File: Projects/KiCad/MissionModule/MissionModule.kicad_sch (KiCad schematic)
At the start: 23 parts, among them J1 Conn_01x04_Pin, J2 Conn_01x04_Pin, J3 Micro_SD_Card_Det_Hirose_DM3AT, U1 ABX00012, U2 MCP2562-E-P, U3 LT1584-3.3, U4 TLP222A, U5 MCP2515-I/P, Y1 8MHz

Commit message: ADXL375のCSをGNDに接続
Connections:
- net GND: now also U6.4 (SDO/ALT_ADDRESS)
- no-connect marks 26 -> 25
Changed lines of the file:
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@@
   (no_connect (at 60.96 118.11))
   (no_connect (at 123.19 161.29))
-  (no_connect (at 82.55 163.83))
   (no_connect (at 60.96 107.95))
   (no_connect (at 60.96 105.41))
@@
   )
   (wire (pts (xy 60.96 107.95) (xy 63.5 107.95))
+    (stroke (width 0) (type default))
+  )
+  (wire (pts (xy 82.55 163.83) (xy 82.55 168.91))
     (stroke (width 0) (type default))
   )
@@
         )
       )
+    )
+  )
+  (symbol (lib_id "power:GND") (at 82.55 168.91 0) (unit 1)
+    (in_bom yes) (on_board yes) (dnp no) (fields_autoplaced)
+    (property "Reference" "#PWR026" (at 82.55 175.26 0)
+      (effects (font (size 1.27 1.27)) hide)
+    )
+    (property "Value" "GND" (at 82.55 173.99 0)
+      (effects (font (size 1.27 1.27)))
+    )
+    (property "Footprint" "" (at 82.55 168.91 0)
+      (effects (font (size 1.27 1.27)) hide)
+    )
+    (property "Datasheet" "" (at 82.55 168.91 0)
+      (effects (font (size 1.27 1.27)) hide)
+    )
+    (pin "1")
+    (instances
+      (project "MissionModule"
+        (path "/ea1ed597-7cd3-4340-902e-bdce8f2d7a62"
+          (reference "#PWR026") (unit 1)
+        )
+      )

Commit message: 全モジュールのkicadを一通り作った
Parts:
- removed C3, C4: 0.1μF, Capacitor_SMD:C_0805_2012Metric_Pad1.18x1.45mm_HandSolder, symbol Device:C
- removed D1: 1N4148, Diode_THT:D_DO-35_SOD27_P7.62mm_Horizontal, symbol Diode:1N4148
- removed U3: LT1584-3.3, Package_TO_SOT_THT:TO-220-3_Vertical, symbol Regulator_Linear:LT1584-3.3
- added C3: 470μF, Capacitor_THT:CP_Radial_D10.0mm_P3.50mm, symbol Device:C_Polarized
- added D1, D2, D3, D4, D5, D6: LED, LED_SMD:LED_1206_3216Metric_Pad1.42x1.75mm_HandSolder, symbol Device:LED
- added R10, R11, R12, R9: 100Ω, Resistor_SMD:R_0805_2012Metric_Pad1.20x1.40mm_HandSolder, symbol Device:R
- added R13: 1kΩ, Resistor_SMD:R_0805_2012Metric_Pad1.20x1.40mm_HandSolder, symbol Device:R
- added R3, R7, R8: 4.7kΩ, Resistor_SMD:R_0805_2012Metric_Pad1.20x1.40mm_HandSolder, symbol Device:R
- added R6: 2kΩ, Resistor_SMD:R_0805_2012Metric_Pad1.20x1.40mm_HandSolder, symbol Device:R
- added SW1, SW2: SW_Push, Button_Switch_THT:SW_PUSH_6mm, symbol Switch:SW_Push
- added U6, U7: MB85RS2MT, Package_DIP:DIP-8_W7.62mm, symbol Memory_NVRAM:MB85RS2MT
- R2: footprint (none) -> Resistor_SMD:R_0805_2012Metric_Pad1.20x1.40mm_HandSolder
- renumbered C5 to C4, C6 to C5, C7 to C6, R3 to R4, R4 to R5, U6 to U1, U1 to U2, U2 to U3
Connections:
- net +3.3V: now also F1.1, C3.1, R3.1, R7.1, R8.1
- net +5V: now also R6.1
- net GND: now also J3.9 (DET_B), C3.2, D1.1 (K), D2.1 (K), D3.1 (K), D4.1 (K), D5.1 (K), D6.1 (K), SW1.1, SW2.1, U6.3 (~{WP}), U6.4 (GND), U6.7 (~{HOLD}), U7.3 (~{WP}), U7.4 (GND), U7.7 (~{HOLD})
- net MEMORY_POWER: now also R13.1, U6.8 (VDD), U7.8 (VDD)
- net SPI_CS_SD: now also R3.2
- net SPI_MISO: now also U6.2 (SO), U7.2 (SO)
- net SPI_MOSI: now also U6.5 (SI), U7.5 (SI)
- net SPI_SCLK: now also U6.6 (SCK), U7.6 (SCK)
- net CAN_SEND_STATUS: now reaches U2.10 (PA23_TC4-W1/1)
- net CAN_SEND_STATUS: now also R10.1
- net RECORD_STATUS: now reaches U2.11 (PA10_TCC0-W2/~2)
- net RECORD_STATUS: now also R11.1
- net SD_CHECK: now reaches U2.12 (PA11_TCC0-W3/~3)
- net SD_CHECK: now also J3.10 (DET_A)
- net SD_STATUS: now reaches U2.13 (PB10_TCC0-W4/~4)
- net SD_STATUS: now also R12.1
- net DUMP_MODE: now reaches U2.5 (PA04_AIN4/A3)
- net DUMP_MODE: now also SW2.2
- net DEBUG_MODE: now reaches U2.6 (PA05_AIN5/A4)
- net DEBUG_MODE: now also SW1.2
- net SPI_CS_FRAM1: now reaches U2.7 (PA06_AIN6/A5)
- net SPI_CS_FRAM1: now also R7.2, U6.1 (~{CS})
- net SPI_CS_FRAM0: now reaches U2.8 (PA07_AIN7/A6)
- net SPI_CS_FRAM0: now also R8.2, U7.1 (~{CS})
- net CAN_RECEIVE_STATUS: now reaches U2.9 (PA22_TC4-W0/0)
- net CAN_RECEIVE_STATUS: now also R9.1
- new net: D1.2 (A), R6.2
- new net: D5.2 (A), R12.2
- new net: D4.2 (A), R11.2
- new net: D3.2 (A), R10.2
- new net: D6.2 (A), R13.2
- new net: D2.2 (A), R9.2
- no-connect marks 25 -> 21
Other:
- moved on the sheet: C1, C2, C4, C5, C6, F1, J3, R1, R2, R4, R5, U1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

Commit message: 一通り部品を選定
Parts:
- added D7, D8: ORANGE, LED_SMD:LED_0603_1608Metric_Pad1.05x0.95mm_HandSolder, symbol Device:LED
- added R14, R15: 100Ω, Resistor_SMD:R_0603_1608Metric_Pad0.98x0.95mm_HandSolder, symbol Device:R
- C3: value 470μF -> 100μF; footprint Capacitor_THT:CP_Radial_D10.0mm_P3.50mm -> Capacitor_SMD:CP_Elec_6.3x7.7
- C5, C6: footprint Capacitor_SMD:C_0805_2012Metric_Pad1.18x1.45mm_HandSolder -> Capacitor_SMD:C_0603_1608Metric_Pad1.08x0.95mm_HandSolder
- D1, D6: value LED -> RED; footprint LED_SMD:LED_1206_3216Metric_Pad1.42x1.75mm_HandSolder -> LED_SMD:LED_0603_1608Metric_Pad1.05x0.95mm_HandSolder
- D2, D3: value LED -> ORANGE; footprint LED_SMD:LED_1206_3216Metric_Pad1.42x1.75mm_HandSolder -> LED_SMD:LED_0603_1608Metric_Pad1.05x0.95mm_HandSolder
- D4, D5: value LED -> GREEN; footprint LED_SMD:LED_1206_3216Metric_Pad1.42x1.75mm_HandSolder -> LED_SMD:LED_0603_1608Metric_Pad1.05x0.95mm_HandSolder
- F1: footprint Fuse:Fuse_BelFuse_0ZRE0005FF_L8.3mm_W3.8mm -> Fuse:Fuse_1206_3216Metric_Pad1.42x1.75mm_HandSolder
- R1: value 120R1/4W -> 120Ω; footprint Resistor_SMD:R_0805_2012Metric_Pad1.20x1.40mm_HandSolder -> Resistor_SMD:R_0603_1608Metric_Pad0.98x0.95mm_HandSolder
- R10, R2, R3, R4, R5, R7, R8, R9: footprint Resistor_SMD:R_0805_2012Metric_Pad1.20x1.40mm_HandSolder -> Resistor_SMD:R_0603_1608Metric_Pad0.98x0.95mm_HandSolder
- R11, R12: value 100Ω -> 300Ω; footprint Resistor_SMD:R_0805_2012Metric_Pad1.20x1.40mm_HandSolder -> Resistor_SMD:R_0603_1608Metric_Pad0.98x0.95mm_HandSolder
- R13: value 1kΩ -> 300Ω; footprint Resistor_SMD:R_0805_2012Metric_Pad1.20x1.40mm_HandSolder -> Resistor_SMD:R_0603_1608Metric_Pad0.98x0.95mm_HandSolder
- R6: value 2kΩ -> 620Ω; footprint Resistor_SMD:R_0805_2012Metric_Pad1.20x1.40mm_HandSolder -> Resistor_SMD:R_0603_1608Metric_Pad0.98x0.95mm_HandSolder
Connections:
- net GND: now also D7.1 (K), D8.1 (K)
- net LORA_SEND_STATUS: now reaches U2.3 (PB02_AIN10/A1)
- net LORA_SEND_STATUS: now also R15.1
- net LORA_RECEIVE_STATUS: now reaches U2.4 (PB03_AIN11/A2)
- net LORA_RECEIVE_STATUS: now also R14.1
- new net: D7.2 (A), R14.2
- new net: D8.2 (A), R15.2
- no-connect marks 21 -> 19
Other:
- moved on the sheet: C1, C2, C4, D1, D2, D3, D4, D5, D6, J1, J2, R1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

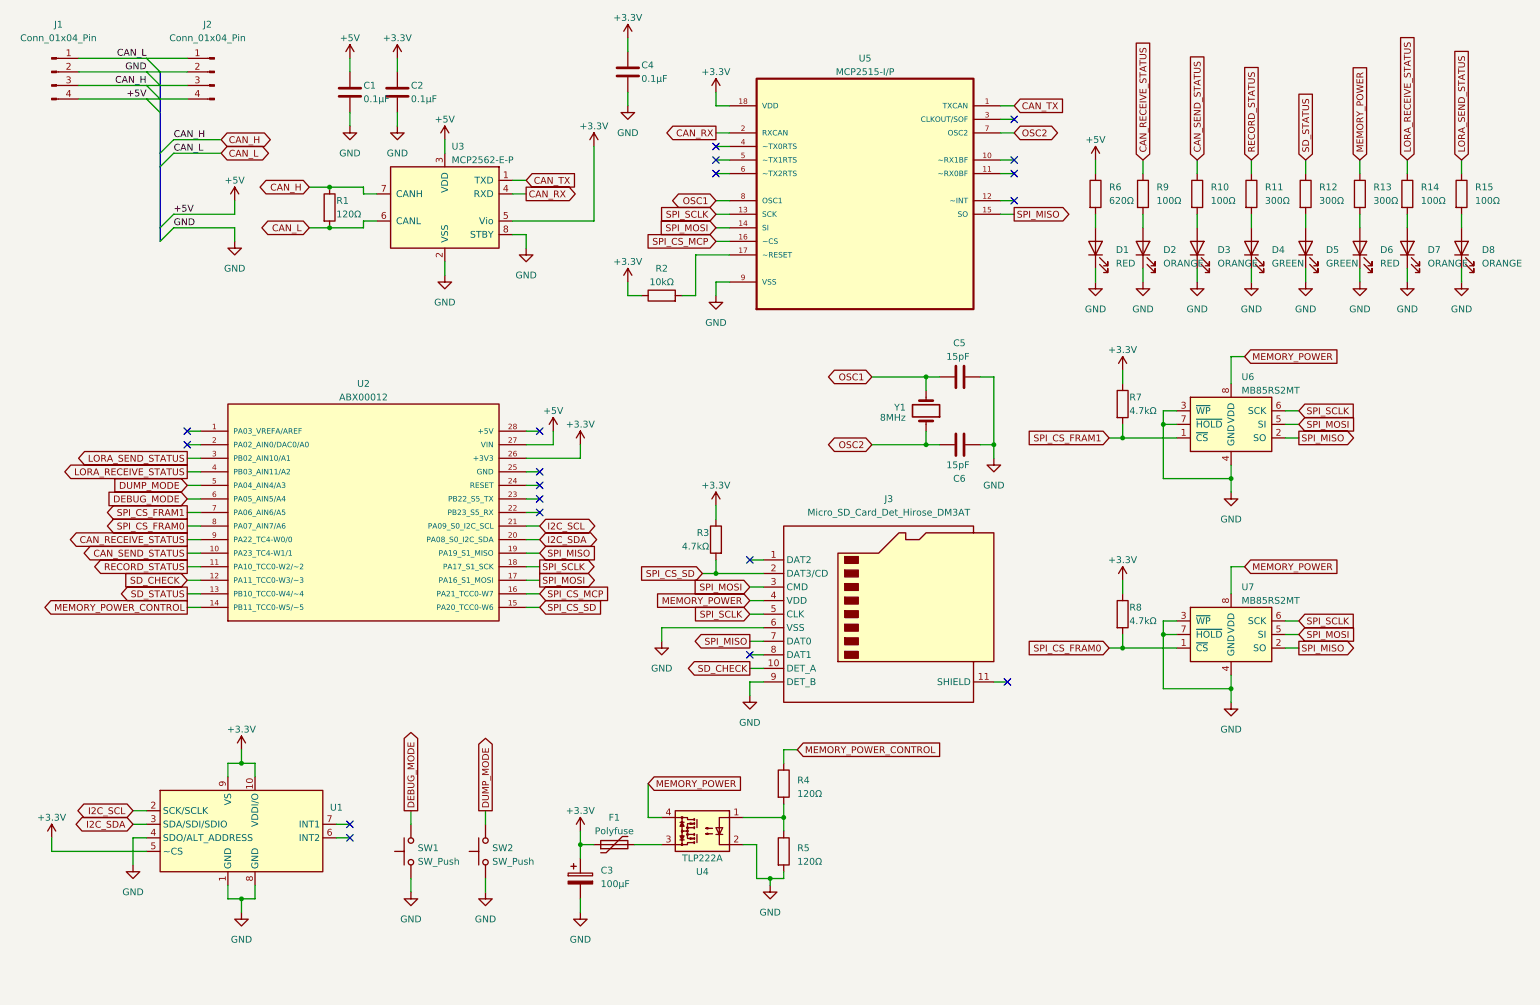
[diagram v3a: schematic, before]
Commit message: コネクタを再配置, 基板上で12V->5Vをするように変更
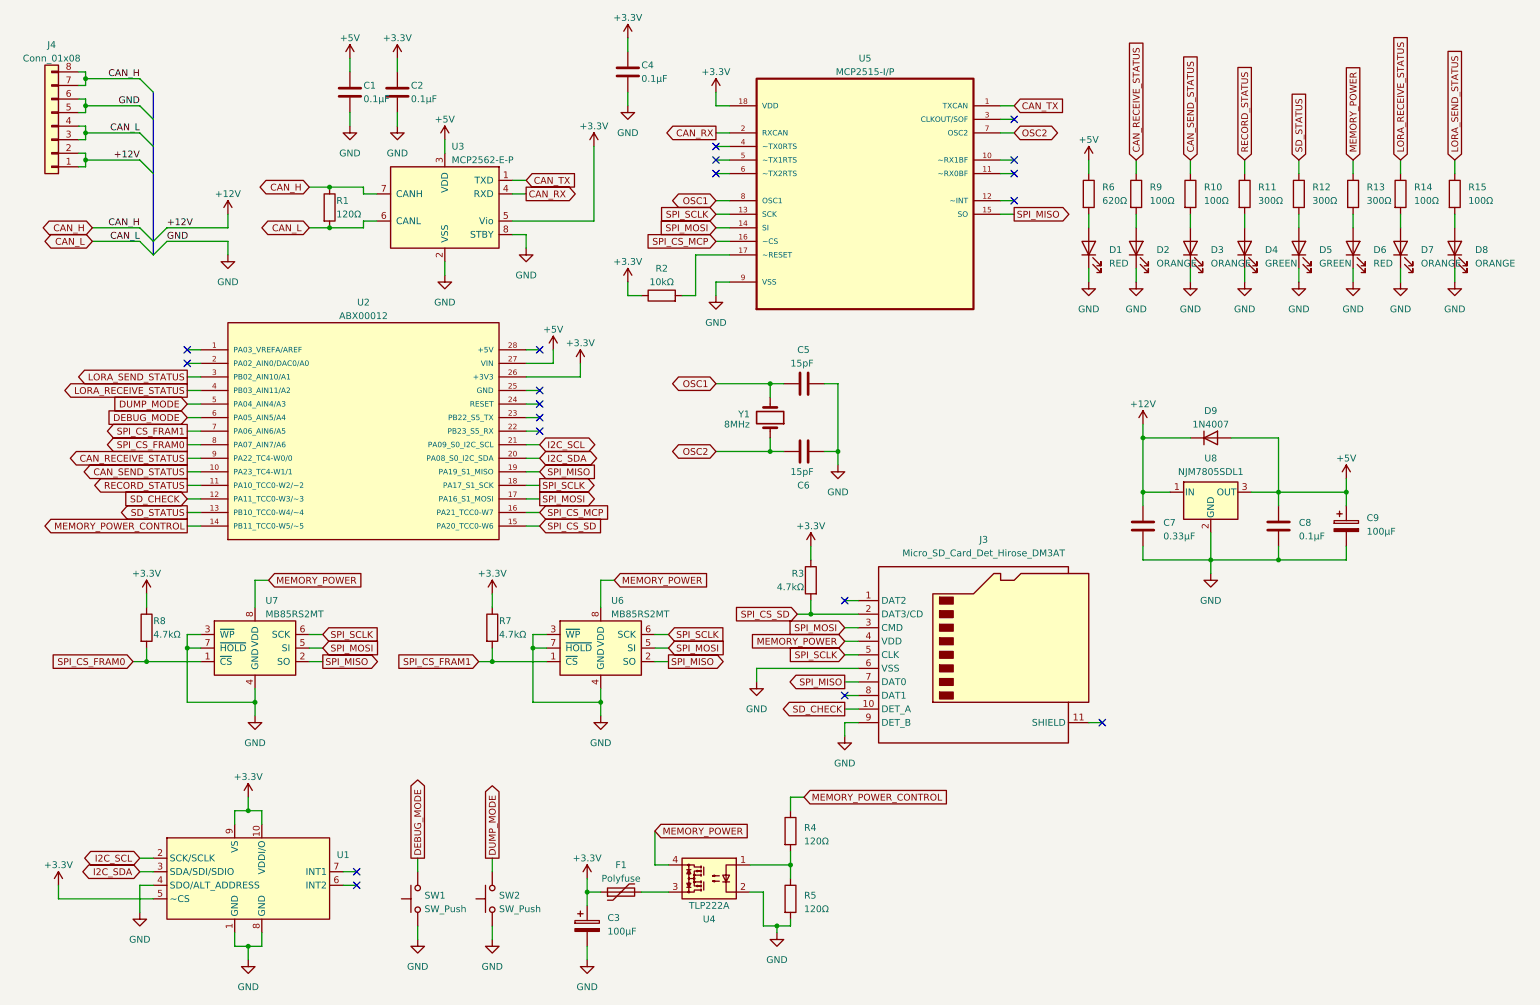
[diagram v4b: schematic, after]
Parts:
- removed J1, J2: Conn_01x04_Pin, Connector_JST:JST_XH_S4B-XH-A_1x04_P2.50mm_Horizontal, symbol Connector:Conn_01x04_Pin
- added C7: 0.33μF, Capacitor_SMD:C_0805_2012Metric_Pad1.18x1.45mm_HandSolder, symbol Device:C
- added C8: 0.1μF, Capacitor_SMD:C_0805_2012Metric_Pad1.18x1.45mm_HandSolder, symbol Device:C
- added C9: 100μF, Capacitor_SMD:CP_Elec_6.3x7.7, symbol Device:C_Polarized
- added D9: 1N4007, Diode_SMD:D_SOD-123F, symbol Diode:1N4007
- added J4: Conn_01x08, Connector_Hirose:Hirose_DF11-8DP-2DSA_2x04_P2.00mm_Vertical, symbol Connector_Generic:Conn_01x08
- added U8: NJM7805SDL1, Package_TO_SOT_SMD:TO-252-3_TabPin2, symbol Regulator_Linear:L7805
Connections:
- net +5V: now also C8.1, C9.1, D9.2 (A), U8.3 (OUT)
- net CAN_H: now also J4.7 (Pin_7), J4.8 (Pin_8)
- net CAN_L: now also J4.3 (Pin_3), J4.4 (Pin_4)
- net GND: now also C7.2, C8.2, C9.2, J4.5 (Pin_5), J4.6 (Pin_6), U8.2 (GND)
- new net +12V: C7.1, D9.1 (K), J4.1 (Pin_1), J4.2 (Pin_2), U8.1 (IN)
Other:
- moved on the sheet: C3, C5, C6, D1, D2, D3, D4, D5, D6, D7, D8, F1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

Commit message: 基板設計の都市伝説をいろいろ適応
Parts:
- U6: renamed from U2; footprint ARDUINO_ABX00012 -> ABX00012:ARDUINO_ABX00012
- renumbered C5 to C1, C1 to C2, C7 to C3, C2 to C4, C4 to C5, C8 to C7, C9 to C8, C3 to C9, D9 to D2, D2 to D3, D3 to D4, D7 to D5, D8 to D6, D4 to D7, D5 to D8, D6 to D9, J4 to J1, J3 to J2, R4 to R10, R3 to R12, R8 to R13, R7 to R14, R12 to R15, R6 to R2, R2 to R3, R9 to R4, R10 to R5, R14 to R6, R15 to R7, R5 to R8, R13 to R9, U3 to U1, U5 to U2, U8 to U3, U1 to U4, U4 to U5, U6 to U7, U7 to U8

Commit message: テストポイントを追加
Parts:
- added TP1, TP2, TP3: TestPoint, Connector_Pin:Pin_D1.0mm_L10.0mm, symbol Connector:TestPoint
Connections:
- net CAN_H: now also TP1.1
- net CAN_L: now also TP2.1
- net MEMORY_POWER: now also TP3.1
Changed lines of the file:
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@@
+    )
+  )
+  (symbol (lib_id "Connector:TestPoint") (at 132.08 166.37 90) (unit 1)
+    (in_bom yes) (on_board yes) (dnp no) (fields_autoplaced)
+    (property "Reference" "TP3" (at 128.778 161.29 90)
+      (effects (font (size 1.27 1.27)))
+    )
+    (property "Value" "TestPoint" (at 128.778 163.83 90)
+      (effects (font (size 1.27 1.27)))
+    )
+    (property "Footprint" "Connector_Pin:Pin_D1.0mm_L10.0mm" (at 132.08 161.29 0)
+      (effects (font (size 1.27 1.27)) hide)
+    )
+    (property "Datasheet" "~" (at 132.08 161.29 0)
+      (effects (font (size 1.27 1.27)) hide)
+    )
+    (pin "1")
+    (instances
+      (project "MissionModule"
+        (path "/ea1ed597-7cd3-4340-902e-bdce8f2d7a62"
+          (reference "TP3") (unit 1)
+        )
+      )
     )
   )
@@
     )
   )
+  (symbol (lib_id "Connector:TestPoint") (at 71.12 45.72 0) (unit 1)
+    (in_bom yes) (on_board yes) (dnp no) (fields_autoplaced)
+    (property "Reference" "TP1" (at 73.66 41.783 0)
+      (effects (font (size 1.27 1.27)) (justify left))
+    )
+    (property "Value" "TestPoint" (at 73.66 44.323 0)
+      (effects (font (size 1.27 1.27)) (justify left))
+    )
+    (property "Footprint" "Connector_Pin:Pin_D1.0mm_L10.0mm" (at 76.2 45.72 0)
+      (effects (font (size 1.27 1.27)) hide)
+    )
+    (property "Datasheet" "~" (at 76.2 45.72 0)
+      (effects (font (size 1.27 1.27)) hide)
+    )
+    (pin "1")
+    (instances
+      (project "MissionModule"
+        (path "/ea1ed597-7cd3-4340-902e-bdce8f2d7a62"
+          (reference "TP1") (unit 1)
+        )
+      )
+    )
+  )
   (symbol (lib_id "Device:R") (at 232.41 46.99 0) (unit 1)
     (in_bom yes) (on_board yes) (dnp no) (fields_autoplaced)
@@
         )
       )
+    )
+  )
+  (symbol (lib_id "Connector:TestPoint") (at 71.12 53.34 180) (unit 1)
+    (in_bom yes) (on_board yes) (dnp no) (fields_autoplaced)
+    (property "Reference" "TP2" (at 73.66 56.007 0)
+      (effects (font (size 1.27 1.27)) (justify right))
+    )
+    (property "Value" "TestPoint" (at 73.66 58.547 0)
+      (effects (font (size 1.27 1.27)) (justify right))
+    )
+    (property "Footprint" "Connector_Pin:Pin_D1.0mm_L10.0mm" (at 66.04 53.34 0)
+      (effects (font (size 1.27 1.27)) hide)
+    )
+    (property "Datasheet" "~" (at 66.04 53.34 0)
+      (effects (font (size 1.27 1.27)) hide)
+    )
+    (pin "1")
+    (instances
+      (project "MissionModule"
+        (path "/ea1ed597-7cd3-4340-902e-bdce8f2d7a62"
+          (reference "TP2") (unit 1)
+        )
+      )

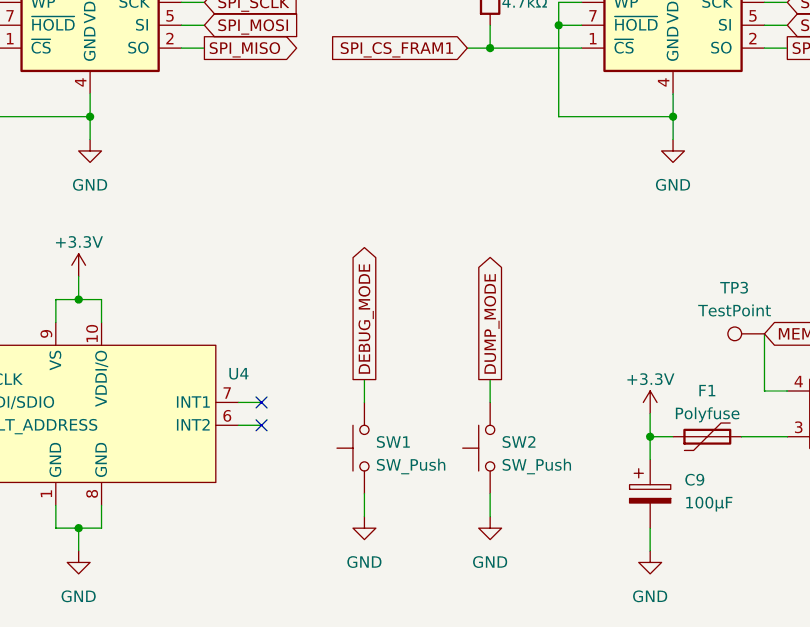
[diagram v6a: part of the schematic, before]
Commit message: スイッチをピアノスイッチに変更
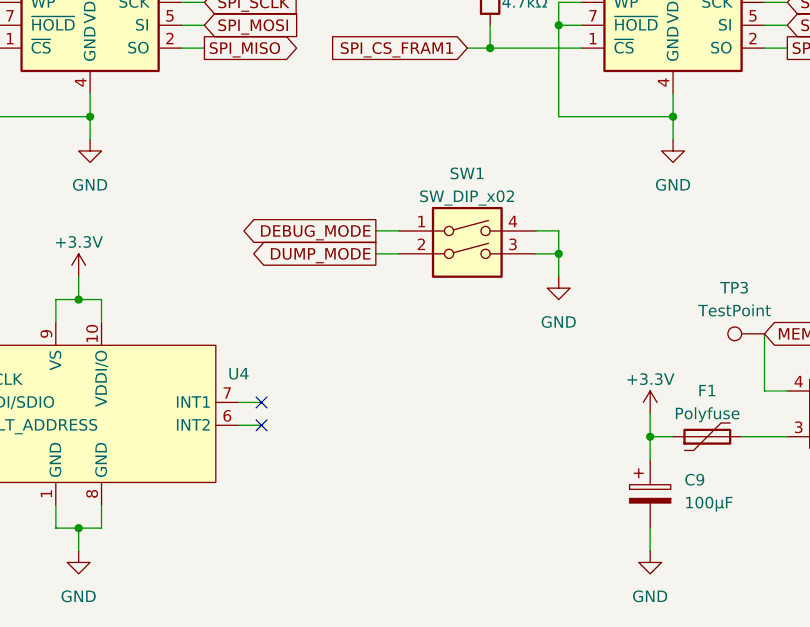
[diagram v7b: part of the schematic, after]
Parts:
- removed SW1, SW2: SW_Push, Button_Switch_THT:SW_PUSH_6mm, symbol Switch:SW_Push
- added SW1: SW_DIP_x02, Button_Switch_THT:SW_DIP_SPSTx02_Piano_10.8x6.64mm_W7.62mm_P2.54mm, symbol Switch:SW_DIP_x02
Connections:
- net DEBUG_MODE: now also SW1.1
- net DUMP_MODE: now also SW1.2
- net GND: now also SW1.3, SW1.4

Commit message: 三端子レギュレータをTO-252-3からTO-252-2に変更
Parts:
- U3: footprint Package_TO_SOT_SMD:TO-252-3_TabPin2 -> Package_TO_SOT_SMD:TO-252-2
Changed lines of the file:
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@@
       (effects (font (size 1.27 1.27)))
     )
-    (property "Footprint" "Package_TO_SOT_SMD:TO-252-3_TabPin2" (at 236.855 106.68 0)
+    (property "Footprint" "Package_TO_SOT_SMD:TO-252-2" (at 236.855 106.68 0)
       (effects (font (size 1.27 1.27) italic) (justify left) hide)
     )
